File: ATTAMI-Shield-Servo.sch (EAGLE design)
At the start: 19 parts

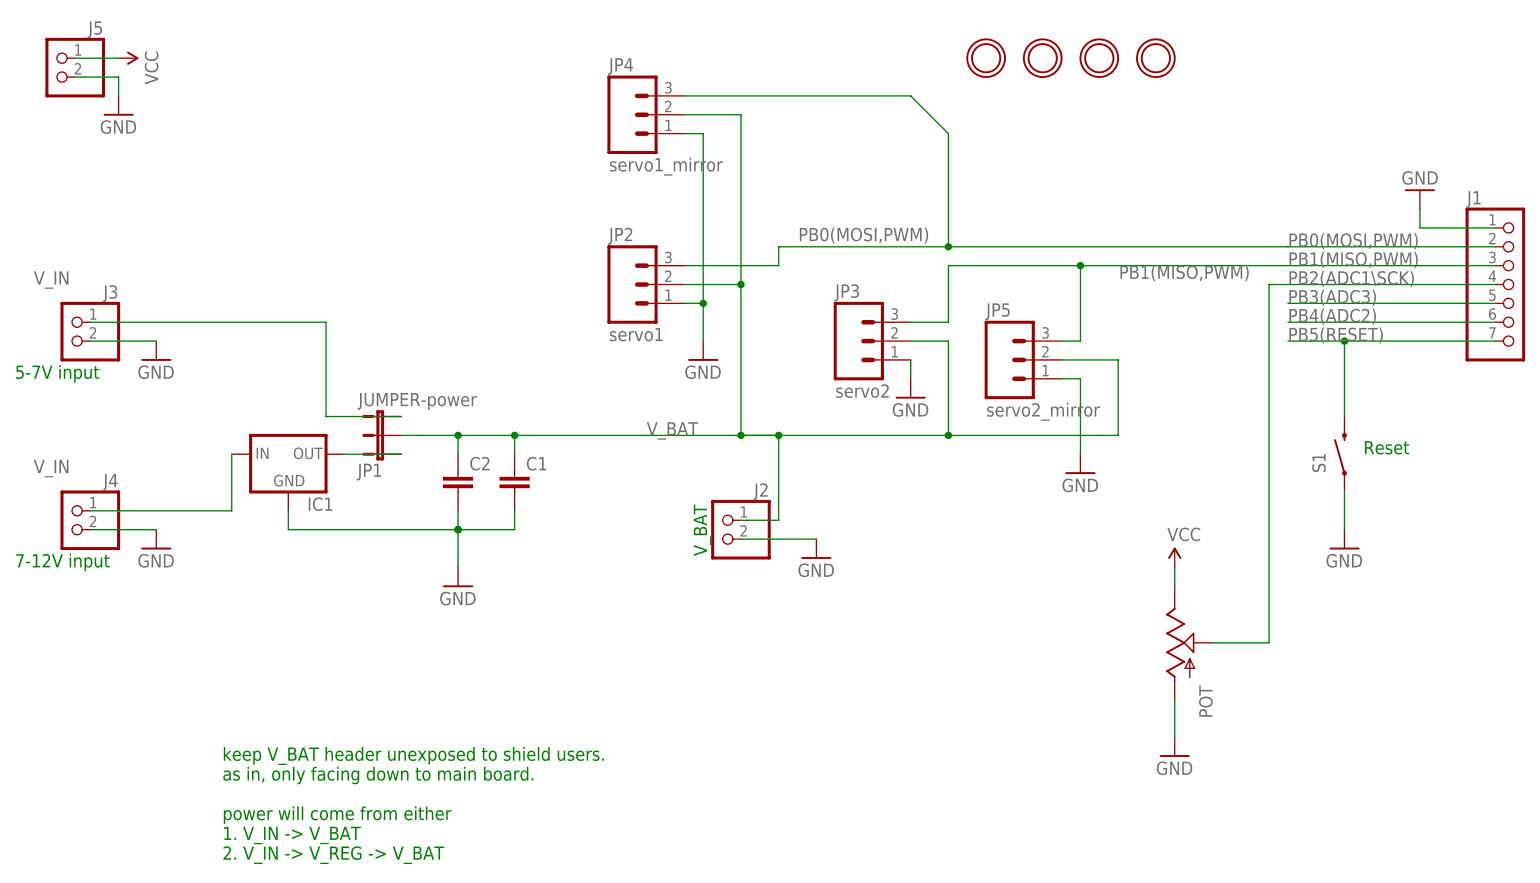
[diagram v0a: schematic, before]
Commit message: midnight edition, 1x2 layout
taking space of two ATTami (1800x900 mil) .
leaving much place for silkscreen.
power on the right, servos on the left
no VCC pins on shield.
bottom copper plate is no longer ground, its now V_BAT.
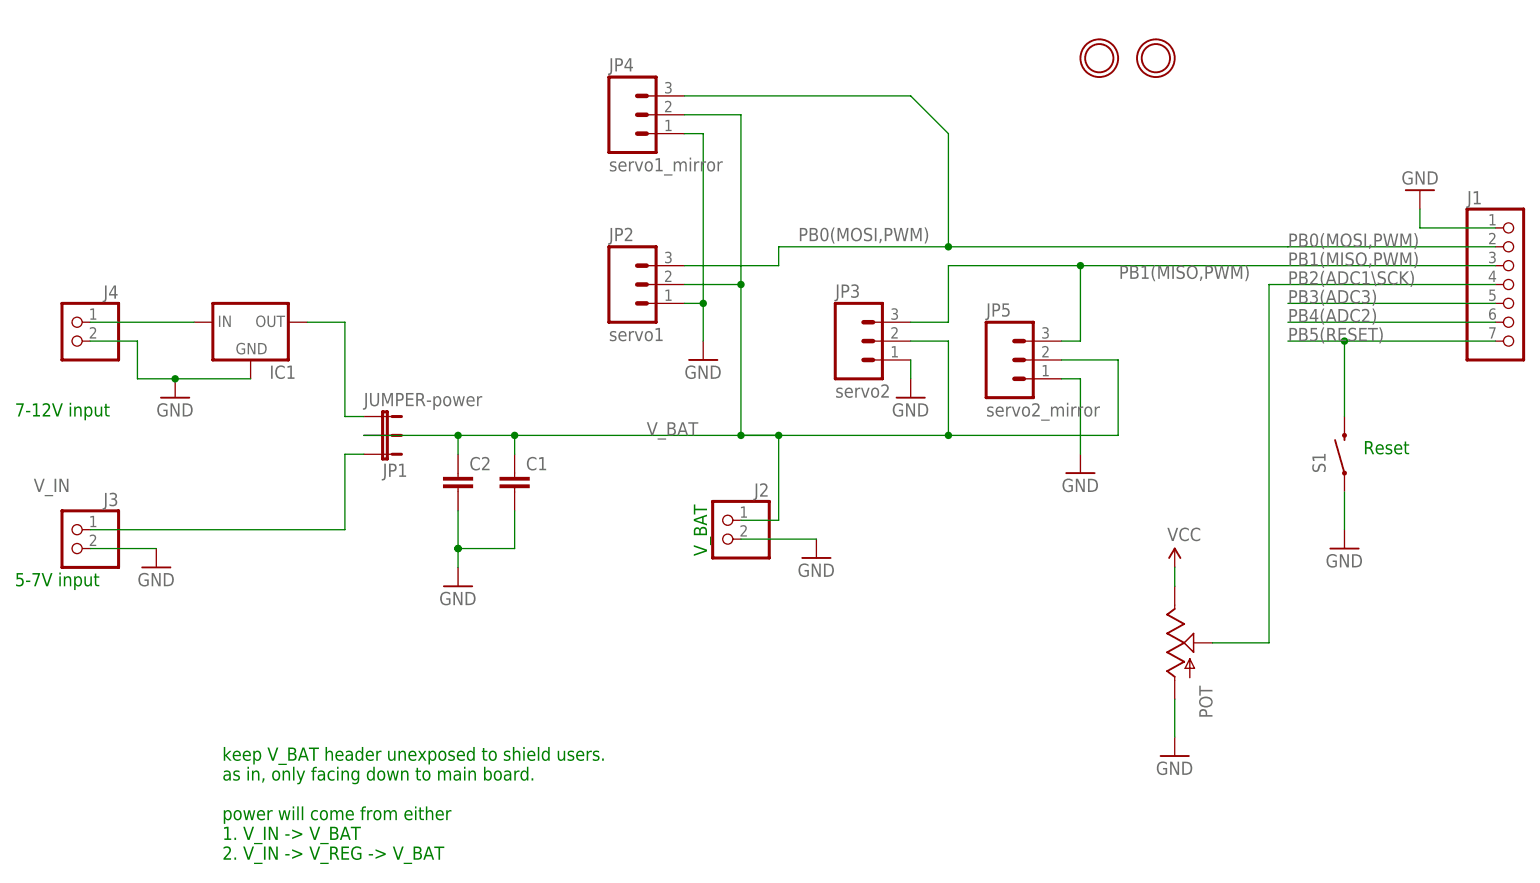
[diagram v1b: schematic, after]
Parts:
- removed J5: (no value), microbuilder:HEADER-1X2ROUND
- removed U$4, U$5: MOUNTINGHOLE2.0, microbuilder:MOUNTINGHOLE2.0
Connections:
- new net N$1: IC1.IN, J4.1
- net GND: no longer J5.2
- net N$3: now also JP1.3; no longer JP1.1
- net VCC: no longer J5.1
- net V_IN: now also JP1.1; no longer IC1.IN, J4.1, JP1.3
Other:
- moved on the sheet: IC1, J3, J4
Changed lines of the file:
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@@
 <part name="JP5" library="SparkFun-Connectors" deviceset="M03" device="LONGPADS" value="servo2_mirror"/>
 <part name="GND13" library="SparkFun" deviceset="GND" device=""/>
-<part name="J5" library="microbuilder" deviceset="HEADER-1X2" device="ROUND"/>
-<part name="SUPPLY1" library="SparkFun-Aesthetics" deviceset="VCC" device=""/>
-<part name="GND14" library="SparkFun" deviceset="GND" device=""/>
-<part name="U$4" library="microbuilder" deviceset="MOUNTINGHOLE" device="2.0" value="MOUNTINGHOLE2.0"/>
-<part name="U$5" library="microbuilder" deviceset="MOUNTINGHOLE" device="2.0" value="MOUNTINGHOLE2.0"/>
 <part name="S1" library="SparkFun-Electromechanical" deviceset="SWITCH-MOMENTARY-2" device="-SMD-1101NE"/>
 <part name="GND15" library="SparkFun" deviceset="GND" device=""/>
@@
 LICENSE: CERN OHL 1.7</text>
 <text x="117.348" y="92.964" size="1.778" layer="91" rot="R90">V_BAT</text>
-<text x="24.13" y="116.84" size="1.778" layer="91">5-7V input</text>
+<text x="24.13" y="88.9" size="1.778" layer="91">5-7V input</text>
 <text x="52.07" y="52.07" size="1.778" layer="91">keep V_BAT header unexposed to shield users.
 as in, only facing down to main board.
@@
 1. V_IN -&gt; V_BAT
 2. V_IN -&gt; V_REG -&gt; V_BAT</text>
-<text x="24.13" y="91.44" size="1.778" layer="91">7-12V input</text>
+<text x="24.13" y="111.76" size="1.778" layer="91">7-12V input</text>
 <text x="205.74" y="106.68" size="1.778" layer="91">Reset</text>
 </plain>
@@
 <instance part="JP2" gate="G$1" x="106.68" y="129.54"/>
 <instance part="JP3" gate="G$1" x="137.16" y="121.92"/>
-<instance part="IC1" gate="G$1" x="60.96" y="106.68"/>
+<instance part="IC1" gate="G$1" x="55.88" y="124.46"/>
 <instance part="C1" gate="G$1" x="91.44" y="101.6"/>
 <instance part="POT" gate="G$1" x="180.34" y="81.28"/>
@@
 <instance part="GND5" gate="1" x="180.34" y="66.04"/>
 <instance part="SUPPLY3" gate="1" x="180.34" y="91.44"/>
-<instance part="JP1" gate="G$1" x="73.66" y="106.68" smashed="yes" rot="R90">
-<attribute name="NAME" x="73.66" y="105.41" size="1.778" layer="95" rot="R180"/>
-<attribute name="VALUE" x="86.36" y="114.935" size="1.778" layer="96" rot="R180"/>
+<instance part="JP1" gate="G$1" x="73.66" y="106.68" smashed="yes" rot="MR90">
+<attribute name="NAME" x="73.66" y="105.41" size="1.778" layer="95" rot="MR180"/>
+<attribute name="VALUE" x="71.12" y="114.935" size="1.778" layer="96" rot="MR180"/>
 </instance>
 <instance part="GND6" gate="1" x="83.82" y="88.9"/>
-<instance part="GND7" gate="1" x="43.18" y="119.38"/>
-<instance part="J3" gate="G$1" x="31.75" y="121.92" rot="MR0"/>
-<instance part="GND8" gate="1" x="43.18" y="93.98"/>
-<instance part="J4" gate="G$1" x="31.75" y="96.52" rot="MR0"/>
+<instance part="GND7" gate="1" x="43.18" y="91.44"/>
+<instance part="J3" gate="G$1" x="31.75" y="93.98" rot="MR0"/>
+<instance part="GND8" gate="1" x="45.72" y="114.3"/>
+<instance part="J4" gate="G$1" x="31.75" y="121.92" rot="MR0"/>
 <instance part="JP4" gate="G$1" x="106.68" y="152.4"/>
 <instance part="JP5" gate="G$1" x="157.48" y="119.38"/>
 <instance part="GND13" gate="1" x="167.64" y="104.14"/>
-<instance part="J5" gate="G$1" x="29.718" y="157.48" rot="MR0"/>
-<instance part="SUPPLY1" gate="1" x="38.1" y="160.02" rot="R270"/>
-<instance part="GND14" gate="1" x="38.1" y="152.4"/>
-<instance part="U$4" gate="G$1" x="162.56" y="160.02"/>
-<instance part="U$5" gate="G$1" x="154.94" y="160.02"/>
 <instance part="S1" gate="G$1" x="203.2" y="106.68" smashed="yes" rot="R90">
 <attribute name="NAME" x="200.66" y="104.14" size="1.778" layer="95" rot="R90"/>
@@
 </segment>
 <segment>
-<wire x1="34.29" y1="121.92" x2="43.18" y2="121.92" width="0.1524" layer="91"/>
+<wire x1="34.29" y1="93.98" x2="43.18" y2="93.98" width="0.1524" layer="91"/>
 <pinref part="GND7" gate="1" pin="GND"/>
 <pinref part="J3" gate="G$1" pin="2"/>
@@
 </segment>
 <segment>
-<pinref part="IC1" gate="G$1" pin="GND"/>
-<wire x1="60.96" y1="99.06" x2="60.96" y2="96.52" width="0.1524" layer="91"/>
-<wire x1="60.96" y1="96.52" x2="83.82" y2="96.52" width="0.1524" layer="91"/>
 <pinref part="GND6" gate="1" pin="GND"/>
-<wire x1="83.82" y1="96.52" x2="83.82" y2="91.44" width="0.1524" layer="91"/>
-<wire x1="83.82" y1="96.52" x2="91.44" y2="96.52" width="0.1524" layer="91"/>
-<junction x="83.82" y="96.52"/>
 <pinref part="C1" gate="G$1" pin="2"/>
-<wire x1="91.44" y1="96.52" x2="91.44" y2="99.06" width="0.1524" layer="91"/>
+<wire x1="91.44" y1="93.98" x2="91.44" y2="99.06" width="0.1524" layer="91"/>
+<wire x1="83.82" y1="93.98" x2="91.44" y2="93.98" width="0.1524" layer="91"/>
+<junction x="83.82" y="93.98"/>
 <pinref part="C2" gate="G$1" pin="2"/>
-<wire x1="83.82" y1="99.06" x2="83.82" y2="96.52" width="0.1524" layer="91"/>
-<junction x="83.82" y="96.52"/>
-</segment>
-<segment>
-<wire x1="34.29" y1="96.52" x2="43.18" y2="96.52" width="0.1524" layer="91"/>
-<pinref part="GND8" gate="1" pin="GND"/>
-<pinref part="J4" gate="G$1" pin="2"/>
+<wire x1="83.82" y1="99.06" x2="83.82" y2="93.98" width="0.1524" layer="91"/>
+<junction x="83.82" y="93.98"/>
+<wire x1="83.82" y1="93.98" x2="83.82" y2="91.44" width="0.1524" layer="91"/>
 </segment>
 <segment>
@@
 </segment>
 <segment>
-<wire x1="32.258" y1="157.48" x2="38.1" y2="157.48" width="0.1524" layer="91"/>
-<pinref part="GND14" gate="1" pin="GND"/>
-<wire x1="38.1" y1="157.48" x2="38.1" y2="154.94" width="0.1524" layer="91"/>
-<pinref part="J5" gate="G$1" pin="2"/>
-</segment>
-<segment>
 <pinref part="S1" gate="G$1" pin="1"/>
 <pinref part="GND15" gate="1" pin="GND"/>
 <wire x1="203.2" y1="101.6" x2="203.2" y2="96.52" width="0.1524" layer="91"/>
 </segment>
+<segment>
+<wire x1="34.29" y1="121.92" x2="40.64" y2="121.92" width="0.1524" layer="91"/>
+<pinref part="J4" gate="G$1" pin="2"/>
+<pinref part="GND8" gate="1" pin="GND"/>
+<wire x1="40.64" y1="121.92" x2="40.64" y2="116.84" width="0.1524" layer="91"/>
+<wire x1="40.64" y1="116.84" x2="45.72" y2="116.84" width="0.1524" layer="91"/>
+<pinref part="IC1" gate="G$1" pin="GND"/>
+<wire x1="55.88" y1="116.84" x2="45.72" y2="116.84" width="0.1524" layer="91"/>
+<junction x="45.72" y="116.84"/>
+</segment>
 </net>
 <net name="VCC" class="0">
@@
 <pinref part="POT" gate="G$1" pin="E"/>
 <wire x1="180.34" y1="91.44" x2="180.34" y2="88.9" width="0.1524" layer="91"/>
-</segment>
-<segment>
-<pinref part="SUPPLY1" gate="1" pin="VCC"/>
-<pinref part="J5" gate="G$1" pin="1"/>
-<wire x1="38.1" y1="160.02" x2="32.258" y2="160.02" width="0.1524" layer="91"/>
 </segment>
 </net>
@@
 <pinref part="JP1" gate="G$1" pin="2"/>
 <label x="109.22" y="109.22" size="1.778" layer="95"/>
-<wire x1="76.2" y1="109.22" x2="83.82" y2="109.22" width="0.1524" layer="91"/>
+<wire x1="71.12" y1="109.22" x2="83.82" y2="109.22" width="0.1524" layer="91"/>
 <wire x1="83.82" y1="109.22" x2="91.44" y2="109.22" width="0.1524" layer="91"/>
 <wire x1="91.44" y1="109.22" x2="121.92" y2="109.22" width="0.1524" layer="91"/>
@@
 <net name="V_IN" class="0">
 <segment>
-<label x="26.67" y="129.54" size="1.778" layer="95"/>
+<label x="26.67" y="101.6" size="1.778" layer="95"/>
+<wire x1="68.58" y1="96.52" x2="34.29" y2="96.52" width="0.1524" layer="91"/>
+<pinref part="J3" gate="G$1" pin="1"/>
+<pinref part="JP1" gate="G$1" pin="1"/>
+<wire x1="71.12" y1="106.68" x2="68.58" y2="106.68" width="0.1524" layer="91"/>
+<wire x1="68.58" y1="106.68" x2="68.58" y2="96.52" width="0.1524" layer="91"/>
+</segment>
+</net>
+<net name="N$1" class="0">
+<segment>
+<pinref part="IC1" gate="G$1" pin="IN"/>
+<pinref part="J4" gate="G$1" pin="1"/>
+<wire x1="48.26" y1="124.46" x2="34.29" y2="124.46" width="0.1524" layer="91"/>
+</segment>
+</net>
+<net name="N$3" class="0">
+<segment>
+<pinref part="IC1" gate="G$1" pin="OUT"/>
+<wire x1="63.5" y1="124.46" x2="68.58" y2="124.46" width="0.1524" layer="91"/>
+<wire x1="68.58" y1="124.46" x2="68.58" y2="111.76" width="0.1524" layer="91"/>
 <pinref part="JP1" gate="G$1" pin="3"/>
-<wire x1="66.04" y1="111.76" x2="76.2" y2="111.76" width="0.1524" layer="91"/>
-<wire x1="66.04" y1="111.76" x2="66.04" y2="124.46" width="0.1524" layer="91"/>
-<wire x1="66.04" y1="124.46" x2="34.29" y2="124.46" width="0.1524" layer="91"/>
-<pinref part="J3" gate="G$1" pin="1"/>
-</segment>
-<segment>
-<label x="26.67" y="104.14" size="1.778" layer="95"/>
-<wire x1="53.34" y1="99.06" x2="34.29" y2="99.06" width="0.1524" layer="91"/>
-<pinref part="J4" gate="G$1" pin="1"/>
-<pinref part="IC1" gate="G$1" pin="IN"/>
-<wire x1="53.34" y1="99.06" x2="53.34" y2="106.68" width="0.1524" layer="91"/>
-</segment>
-</net>
-<net name="N$3" class="0">
-<segment>
-<pinref part="IC1" gate="G$1" pin="OUT"/>
-<pinref part="JP1" gate="G$1" pin="1"/>
-<wire x1="76.2" y1="106.68" x2="68.58" y2="106.68" width="0.1524" layer="91"/>
-</segment>
-</net>
+<wire x1="68.58" y1="111.76" x2="71.12" y2="111.76" width="0.1524" layer="91"/>
+</segment>
+</net>
